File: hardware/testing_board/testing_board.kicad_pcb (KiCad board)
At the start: 2 copper layers, 68 parts, among them J1 Conn_01x04, J10 Conn_01x02, J11 Conn_01x02, J12 Conn_01x02, J13 Conn_01x02, J14 Conn_01x02, J15 Conn_01x02, J16 Conn_01x04, J2 Conn_01x04, J3 Conn_01x04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

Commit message: update testing board
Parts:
- added R26: 330, Resistor_THT:R_Axial_DIN0204_L3.6mm_D1.6mm_P2.54mm_Vertical, F.Cu at (88.3, 8.26)
- R10, R12, R8, R9: value 220 -> 1k
- moved D10 362.0 mm to (-26.7, 12.7), turned to 270 degrees
- moved R16 348.0 mm to (-5.08, 15.2), turned to 90 degrees
- moved D17 340.4 mm to (-17.8, 22.9), turned to 90 degrees
- moved J14 339.3 mm to (-27.9, 30.5), turned to 180 degrees
- moved J7 338.0 mm to (-44.5, 5.08)
- moved D12 334.0 mm to (1.27, 12.7), turned to 270 degrees
- moved J10 333.2 mm to (-2.54, 5.08)
- moved D16 333.1 mm to (-31.8, 22.9), turned to 90 degrees
- moved D11 332.8 mm to (-12.7, 12.7), turned to 270 degrees
- moved R13 331.0 mm to (-47.0, 15.2), turned to 90 degrees
- moved R15 330.4 mm to (-19.1, 15.2), turned to 90 degrees
- moved J9 329.0 mm to (-16.5, 5.08)
- moved R24 328.9 mm to (-11.4, 20.3), turned to 270 degrees
- moved J13 326.4 mm to (-14.0, 30.5), turned to 180 degrees
- moved R23 326.3 mm to (-25.4, 20.3), turned to 270 degrees
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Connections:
- D1 pad 2: Net-(D1-Pad1) -> Net-(D1-Pad2)
- J3 pad 3: +5V -> Net-(J3-Pad3)
- J4 pad 3: +5V -> Net-(J4-Pad3)
- R1 pad 2: Net-(D1-Pad1) -> Net-(D1-Pad2)
- RV1 pad 3: GND -> Net-(R26-Pad2)
- RV2 pad 3: GND -> Net-(R26-Pad2)
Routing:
- net +5V: track 0.00 -> 78.7 mm
- net Net-(R17-Pad2): track 0.00 -> 26.9 mm
- net Net-(J16-Pad2): track 0.00 -> 24.2 mm
- net Net-(R26-Pad2): track 0.00 -> 21.4 mm
- net Net-(D8-Pad2): track 0.00 -> 19.9 mm
- net Net-(D3-Pad2): track 0.00 -> 19.8 mm
- net Net-(D13-Pad2): track 0.00 -> 19.7 mm
- net Net-(J5-Pad2): track 0.00 -> 19.2 mm
- net Net-(D14-Pad2): track 0.00 -> 19.2 mm
- net Net-(J5-Pad1): track 0.00 -> 14.9 mm
- net Net-(J11-Pad1): track 0.00 -> 14.3 mm
- net Net-(J11-Pad2): track 0.00 -> 13.9 mm
- net GND: track 0.00 -> 8.89 mm
- net Net-(J14-Pad1): track 0.00 -> 8.67 mm
- net Net-(J13-Pad1): track 0.00 -> 8.67 mm
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
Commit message: finish prelimary version of training board
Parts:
- removed J10, J11, J12, J13, J14, J15: Conn_01x02, Connector_JST:JST_XH_B2B-XH-A_1x02_P2.50mm_Vertical
- added D19: DIODE, Diode_THT:D_DO-27_P15.24mm_Horizontal, F.Cu at (89.4, 97.4)
- added D20: DIODE, Diode_THT:D_DO-27_P15.24mm_Horizontal, F.Cu at (68.5, 97.4)
- added D21: LED, LED_THT:LED_D3.0mm, F.Cu at (94.6, 132.0)
- added D22: LED, LED_THT:LED_D3.0mm, F.Cu at (72.4, 132.1)
- added R27: 560, Resistor_THT:R_Axial_DIN0204_L3.6mm_D1.6mm_P2.54mm_Vertical, F.Cu at (49.1, 131.7)
- added R28: 560, Resistor_THT:R_Axial_DIN0204_L3.6mm_D1.6mm_P2.54mm_Vertical, F.Cu at (101.0, 132.0)
- added RLY2: G5LE-14_DC5, digikey-footprints:Relay_THT_G5LE-14, F.Cu at (76.1, 105.9)
- added U3: TPIC6595, Package_DIP:DIP-20_W7.62mm_LongPads, F.Cu at (27.9, 104.6)
- J6, J7, J8, J9: value Conn_01x02 -> Conn_01x04; footprint Connector_JST:JST_XH_B2B-XH-A_1x02_P2.50mm_Vertical -> Connector_JST:JST_XH_B4B-XH-A_1x04_P2.50mm_Vertical
- RLY1: value G5V-1-DC12 -> G5LE-14_DC5; footprint digikey-footprints:Relay_THT_G5V-1 -> digikey-footprints:Relay_THT_G5LE-14
- moved J16 184.0 mm to (110.1, 145.4), turned to 90 degrees
- moved R18 182.6 mm to (102.5, 146.7), turned to 0 degrees
- moved U1 175.6 mm to (102.5, 141.6), turned to 90 degrees
- moved J5 172.8 mm to (80.9, 173.9)
- moved U2 172.6 mm to (93.6, 141.6), turned to 90 degrees
- moved R19 159.4 mm to (81.4, 167.0), turned to 90 degrees
- moved R17 158.9 mm to (85.2, 167.0), turned to 90 degrees
- moved R26 158.8 mm to (89.0, 167.0), turned to 90 degrees
- moved RV2 147.0 mm to (80.1, 160.7), turned to 90 degrees
- moved RV1 146.7 mm to (95.4, 160.7), turned to 90 degrees
- moved RLY1 142.4 mm to (97.2, 105.9)
- moved J4 141.6 mm to (23.2, 129.8), turned to 270 degrees
- moved D15 140.4 mm to (61.7, 113.3), turned to 180 degrees
- moved R7 140.0 mm to (28.6, 137.9), turned to 90 degrees
- moved R22 139.6 mm to (60.3, 118.1)
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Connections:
- J2 pad 1: Net-(J2-Pad1) -> Net-(D8-Pad1)
- J2 pad 2: Net-(J2-Pad2) -> Net-(D3-Pad1)
- J7 pad 2: Net-(D9-Pad1) -> Net-(J7-Pad2)
- J8 pad 2: Net-(D10-Pad1) -> Net-(J8-Pad2)
- J9 pad 1: Net-(J9-Pad1) -> Net-(D19-Pad2)
- J9 pad 2: Net-(D11-Pad1) -> Net-(D20-Pad2)
- R10 pad 2: Net-(D8-Pad2) -> Net-(D8-Pad1)
- R11 pad 1: Net-(J2-Pad1) -> Net-(D8-Pad2)
- R11 pad 2: Net-(D8-Pad1) -> Net-(R11-Pad2)
- R13 pad 2: Net-(J7-Pad1) -> +5V
- R14 pad 2: Net-(J8-Pad1) -> +5V
- R15 pad 2: Net-(J9-Pad1) -> +5V
- R16 pad 2: Net-(J10-Pad1) -> +5V
- R20 pad 1: Net-(D13-Pad1) -> Net-(D22-Pad1)
- R20 pad 2: Net-(D14-Pad2) -> GND
- R22 pad 2: Net-(J15-Pad1) -> +5V
- R23 pad 2: Net-(J14-Pad1) -> +5V
- R24 pad 2: Net-(J13-Pad1) -> +5V
- R25 pad 2: Net-(J12-Pad1) -> +5V
- R3 pad 1: Net-(J2-Pad2) -> Net-(R3-Pad1)
- R3 pad 2: Net-(D3-Pad1) -> Net-(D3-Pad2)
- R9 pad 2: Net-(D3-Pad2) -> Net-(D3-Pad1)
- RLY1 pad 1: Net-(RLY1-Pad1) -> +5V
- RLY1 pad 2: Net-(J11-Pad1) -> GND
- RLY1 pad 5: Net-(RLY1-Pad5) -> Net-(D19-Pad2)
- SW3 pad 2: Net-(D3-Pad2) -> Net-(R3-Pad1)
- SW4 pad 2: Net-(D8-Pad2) -> Net-(R11-Pad2)
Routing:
- net +5V: track 78.7 -> 272.0 mm
- net Net-(J7-Pad1): track 8.67 -> 45.7 mm, vias 0 -> 2
- net Net-(D19-Pad2): track 0.00 -> 29.5 mm
- net Net-(D10-Pad1): track 8.16 -> 35.1 mm
- net Net-(D9-Pad1): track 8.16 -> 33.8 mm, vias 0 -> 1
- net Net-(J7-Pad2): track 0.00 -> 22.2 mm
- net Net-(D11-Pad1): track 8.16 -> 30.0 mm
- net Net-(R2-Pad2): track 0.00 -> 21.5 mm
- net Net-(R1-Pad1): track 0.00 -> 21.3 mm
- net Net-(D20-Pad2): track 0.00 -> 21.2 mm
- net Net-(R3-Pad1): track 0.00 -> 18.7 mm
- net Net-(R11-Pad2): track 0.00 -> 18.6 mm
- net Net-(D12-Pad1): track 8.16 -> 26.7 mm
- net Net-(D2-Pad1): track 0.00 -> 16.8 mm
- net Net-(D1-Pad1): track 0.00 -> 15.9 mm
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- added copper zone on B.Cu, net GND
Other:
- board outline added: 100.6 x 99.1 mm

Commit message: update testing board and start work on piezo amplifier
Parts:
- D19, D20: value DIODE -> D_Schottky; footprint Diode_THT:D_DO-27_P15.24mm_Horizontal -> Diode_THT:D_DO-201AE_P15.24mm_Horizontal
- moved D20 15.4 mm to (83.8, 97.8), turned to 180 degrees
- moved D19 15.0 mm to (104.4, 97.8), turned to 180 degrees
- moved R21 5.25 mm to (51.8, 131.6), turned to 180 degrees
- moved R27 4.97 mm to (51.8, 135.9), turned to 180 degrees
- moved D14 2.29 mm to (43.9, 131.3), turned to 90 degrees
- moved D13 0.25 mm to (43.9, 135.6)
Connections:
- D19 pad 1: GND -> Net-(D19-Pad1)
- D19 pad 2: Net-(D19-Pad2) -> GND
- D20 pad 1: GND -> Net-(D20-Pad1)
- D20 pad 2: Net-(D20-Pad2) -> GND
- J6 pad 1: Net-(D13-Pad2) -> Net-(D14-Pad1)
- J6 pad 2: Net-(D14-Pad2) -> Net-(D13-Pad1)
- J9 pad 1: Net-(D19-Pad2) -> Net-(D19-Pad1)
- J9 pad 2: Net-(D20-Pad2) -> Net-(D20-Pad1)
- R21 pad 1: Net-(D14-Pad1) -> Net-(D13-Pad1)
- R21 pad 2: Net-(D13-Pad2) -> Net-(D14-Pad2)
- R27 pad 1: Net-(D13-Pad1) -> Net-(D14-Pad1)
- R27 pad 2: Net-(D14-Pad2) -> Net-(D13-Pad2)
- RLY1 pad 5: Net-(D19-Pad2) -> Net-(D19-Pad1)
- RLY2 pad 5: Net-(D20-Pad2) -> Net-(D20-Pad1)
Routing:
- net Net-(D19-Pad2): track 29.5 -> 0.00 mm
- net Net-(D19-Pad1): track 0.00 -> 28.9 mm
- net Net-(D20-Pad2): track 21.2 -> 0.00 mm
- net Net-(D20-Pad1): track 0.00 -> 21.2 mm
- net Net-(D14-Pad2): track 16.7 -> 6.49 mm
- net Net-(D13-Pad1): track 6.73 -> 16.6 mm
- net Net-(D13-Pad2): track 15.5 -> 6.28 mm
- net Net-(D14-Pad1): track 19.3 -> 16.0 mm

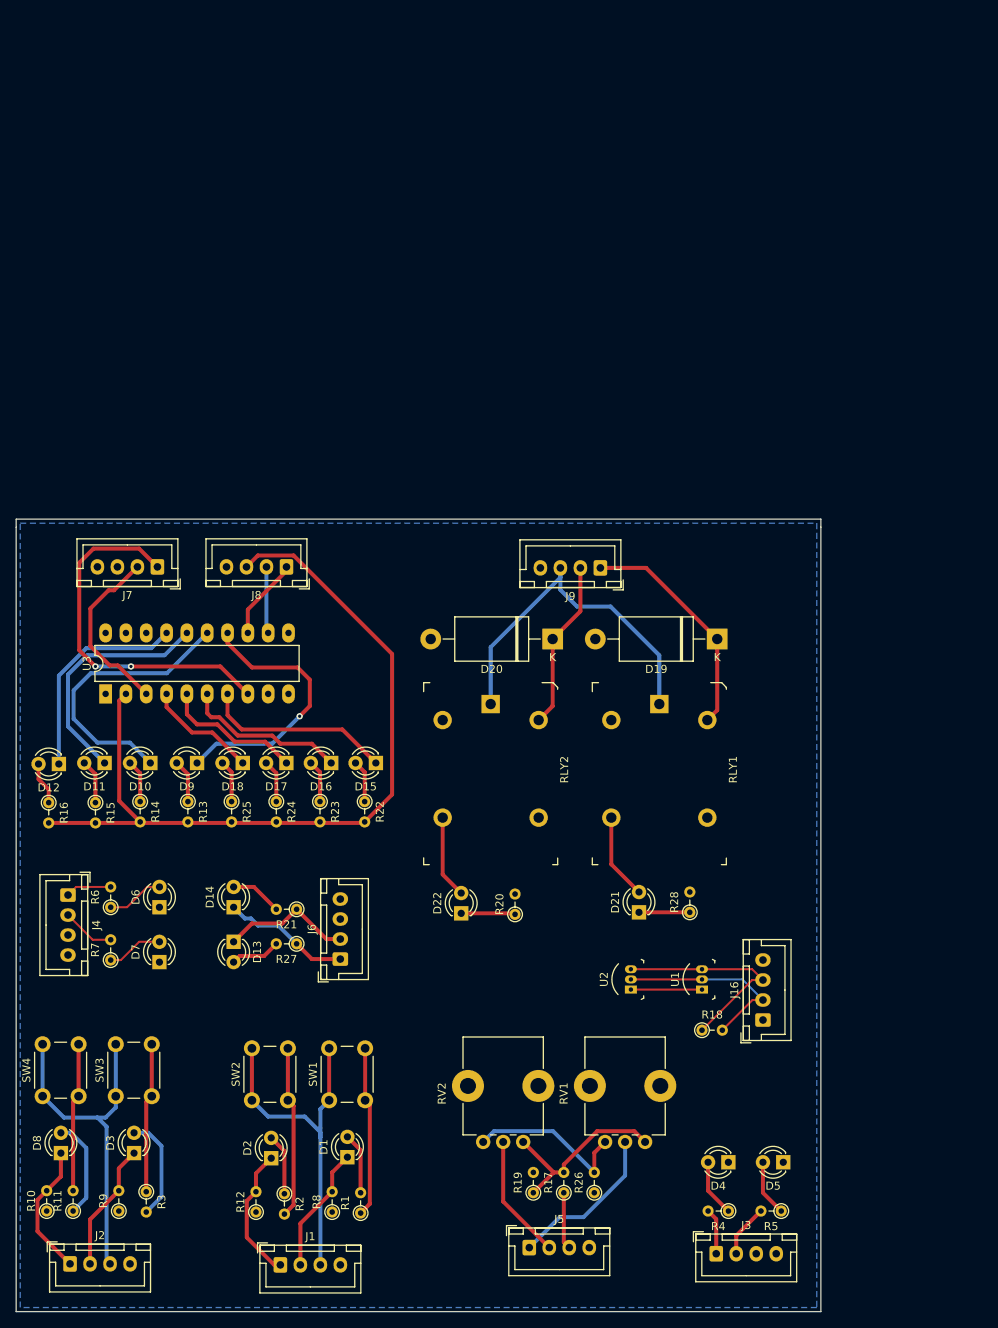
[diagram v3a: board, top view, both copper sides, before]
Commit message: Add mounting holes and spacers
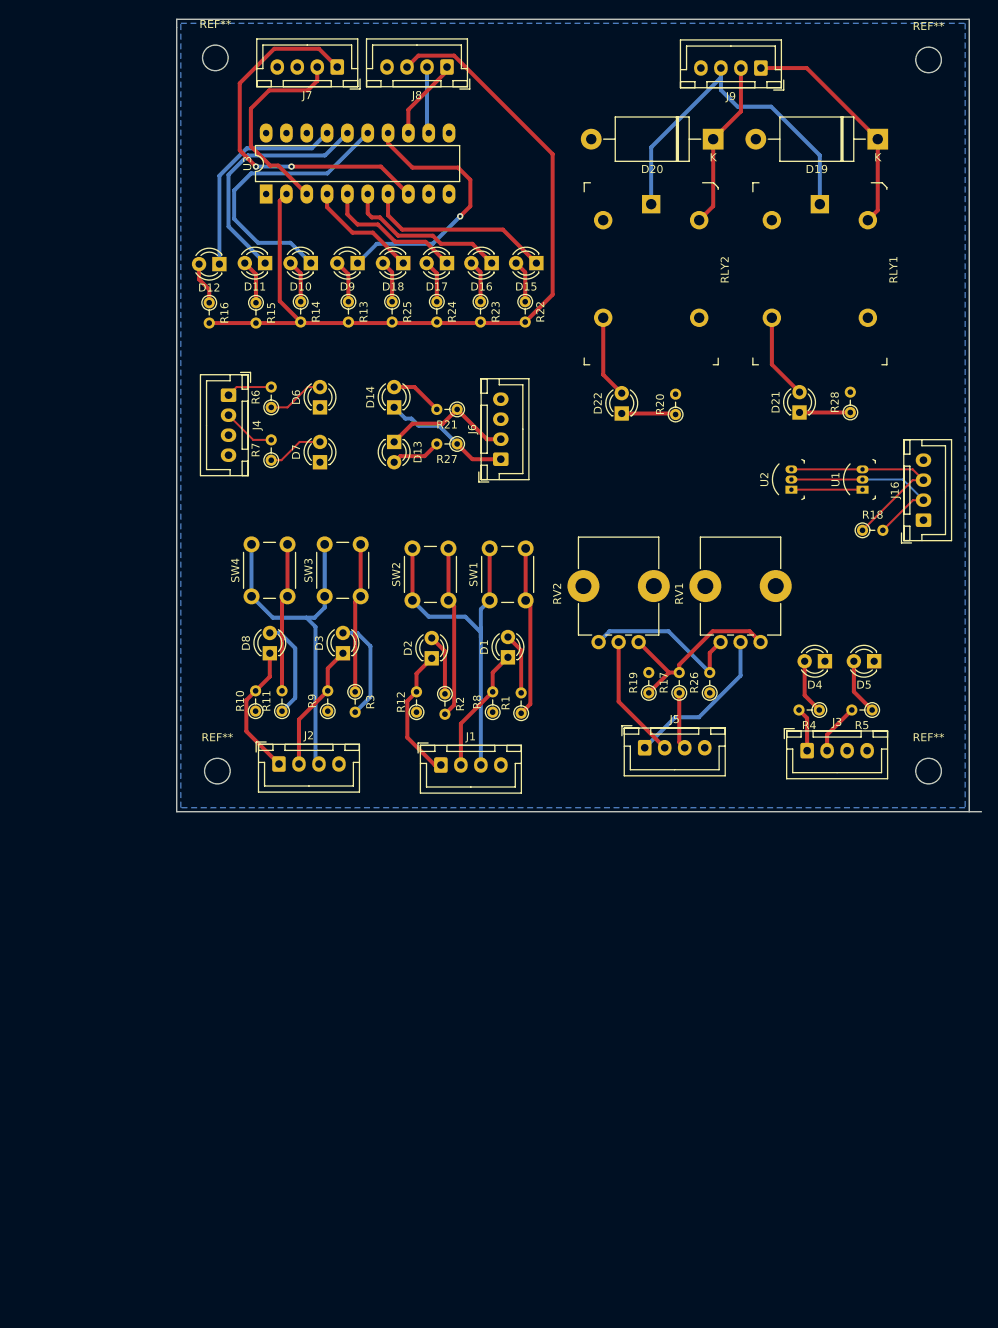
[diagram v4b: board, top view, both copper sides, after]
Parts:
- added REF**: MountingHole_3.2mm_M3, MountingHole:MountingHole_3.2mm_M3, F.Cu at (130.8, 114.3)
- added REF**: MountingHole_3.2mm_M3, MountingHole:MountingHole_3.2mm_M3, F.Cu at (130.8, 25.4)
- added REF**: MountingHole_3.2mm_M3, MountingHole:MountingHole_3.2mm_M3, F.Cu at (41.7, 25.1)
- added REF**: MountingHole_3.2mm_M3, MountingHole:MountingHole_3.2mm_M3, F.Cu at (41.9, 114.3)
- moved J2 67.7 mm to (49.6, 113.4)
- moved D3 67.7 mm to (57.6, 99.6)
- moved D8 67.7 mm to (48.5, 99.6)
- moved R10 67.7 mm to (46.7, 106.8)
- moved R11 67.7 mm to (50.0, 106.8)
- moved R9 67.7 mm to (55.7, 106.8)
- moved SW3 67.7 mm to (55.3, 92.5)
- moved SW4 67.7 mm to (46.2, 92.5)
- moved R3 67.7 mm to (59.1, 104.4)
- moved J7 66.4 mm to (56.9, 26.3)
- moved D1 65.6 mm to (78.2, 100.1)
- moved D10 65.6 mm to (53.6, 50.8)
- moved D11 65.6 mm to (47.9, 50.8)
- moved D14 65.6 mm to (64.0, 68.8)
- moved D15 65.6 mm to (81.8, 50.8)
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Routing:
- net Net-(J7-Pad2): track 22.2 -> 25.6 mm
- net Net-(J7-Pad1): track 45.7 -> 46.7 mm
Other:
- outline, holes or cut-outs redrawn
- net class Default removed

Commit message: update training bpoard design
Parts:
- removed REF** (x4): MountingHole_3.2mm_M3, MountingHole:MountingHole_3.2mm_M3
- added H1: MountingHole, MountingHole:MountingHole_3.2mm_M3_DIN965, F.Cu at (41.7, 25.1)
- added H2: MountingHole, MountingHole:MountingHole_3.2mm_M3_DIN965, F.Cu at (130.8, 25.4)
- added H3: MountingHole, MountingHole:MountingHole_3.2mm_M3_DIN965, F.Cu at (41.9, 114.3)
- added H4: MountingHole, MountingHole:MountingHole_3.2mm_M3_DIN965, F.Cu at (130.8, 114.3)
- moved J3 78.0 mm to (43.2, 82.9), turned to -90 degrees
- moved R5 77.1 mm to (48.2, 91.0), turned to 90 degrees
- moved R4 72.4 mm to (48.2, 84.4), turned to 90 degrees
- moved D5 70.3 mm to (54.3, 91.3), turned to 90 degrees
- moved J16 70.1 mm to (88.4, 26.6), turned to 180 degrees
- moved D4 65.4 mm to (54.3, 85.1), turned to 90 degrees
- moved R18 63.8 mm to (82.2, 34.8)
- moved U1 52.4 mm to (84.7, 42.9), turned to 180 degrees
- moved R21 42.7 mm to (48.4, 104.7), turned to 0 degrees
- moved J6 41.5 mm to (42.9, 98.5), turned to -90 degrees
- moved U2 41.3 mm to (84.7, 49.6), turned to 180 degrees
- moved D14 36.9 mm to (56.2, 105.0), turned to -90 degrees
- moved R27 35.8 mm to (48.4, 100.4), turned to 0 degrees
- moved D13 28.6 mm to (56.2, 100.6), turned to 90 degrees
- moved R16 23.2 mm to (56.1, 38.2), turned to 0 degrees
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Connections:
- D10 pad 1: Net-(D10-Pad1) -> Net-(R14-Pad1)
- D10 pad 2: Net-(D10-Pad2) -> +5V
- D11 pad 2: Net-(D11-Pad2) -> +5V
- D12 pad 1: Net-(D12-Pad1) -> Net-(R16-Pad1)
- D12 pad 2: Net-(D12-Pad2) -> +5V
- D13 pad 1: Net-(D13-Pad1) -> GND
- D14 pad 1: Net-(D14-Pad1) -> GND
- D15 pad 2: Net-(D15-Pad2) -> +5V
- D16 pad 2: Net-(D16-Pad2) -> +5V
- D17 pad 2: Net-(D17-Pad2) -> +5V
- D18 pad 1: Net-(D18-Pad1) -> Net-(R25-Pad1)
- D18 pad 2: Net-(D18-Pad2) -> +5V
- D9 pad 2: Net-(D9-Pad2) -> +5V
- J16 pad 1: Net-(J16-Pad1) -> unconnected-(J16-Pad1)
- J3 pad 3: Net-(J3-Pad3) -> +5V
- J4 pad 3: Net-(J4-Pad3) -> +5V
- J6 pad 1: Net-(D14-Pad1) -> Net-(J6-Pad1)
- J6 pad 2: Net-(D13-Pad1) -> Net-(J6-Pad2)
- R13 pad 1: Net-(D9-Pad2) -> Net-(D9-Pad1)
- R13 pad 2: +5V -> Net-(U3-Pad14)
- R14 pad 1: Net-(D10-Pad2) -> Net-(R14-Pad1)
- R14 pad 2: +5V -> Net-(U3-Pad15)
- R15 pad 1: Net-(D11-Pad2) -> Net-(D11-Pad1)
- R15 pad 2: +5V -> Net-(U3-Pad16)
- R16 pad 1: Net-(D12-Pad2) -> Net-(R16-Pad1)
- R16 pad 2: +5V -> Net-(U3-Pad17)
- R21 pad 1: Net-(D13-Pad1) -> Net-(J6-Pad2)
- R22 pad 1: Net-(D15-Pad2) -> Net-(D15-Pad1)
- R22 pad 2: +5V -> Net-(U3-Pad7)
- R23 pad 1: Net-(D16-Pad2) -> Net-(D16-Pad1)
- R23 pad 2: +5V -> Net-(U3-Pad6)
- R24 pad 1: Net-(D17-Pad2) -> Net-(D17-Pad1)
- R24 pad 2: +5V -> Net-(R24-Pad2)
- R25 pad 1: Net-(D18-Pad2) -> Net-(R25-Pad1)
- R25 pad 2: +5V -> Net-(U3-Pad4)
- R27 pad 1: Net-(D14-Pad1) -> Net-(J6-Pad1)
- RLY1 pad 4: Net-(RLY1-Pad4) -> unconnected-(RLY1-Pad4)
- RLY2 pad 4: Net-(RLY2-Pad4) -> unconnected-(RLY2-Pad4)
- U3 pad 14: Net-(D9-Pad1) -> Net-(U3-Pad14)
- U3 pad 15: Net-(D10-Pad1) -> Net-(U3-Pad15)
- U3 pad 16: Net-(D11-Pad1) -> Net-(U3-Pad16)
- U3 pad 17: Net-(D12-Pad1) -> Net-(U3-Pad17)
- U3 pad 18: Net-(U3-Pad18) -> unconnected-(U3-Pad18)
- U3 pad 4: Net-(D18-Pad1) -> Net-(U3-Pad4)
- U3 pad 5: Net-(D17-Pad1) -> Net-(R24-Pad2)
- U3 pad 6: Net-(D16-Pad1) -> Net-(U3-Pad6)
- U3 pad 7: Net-(D15-Pad1) -> Net-(U3-Pad7)
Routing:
- net +5V: track 272.0 -> 192.4 mm
- net Net-(J7-Pad1): track 46.7 -> 0.00 mm, vias 2 -> 0
- net Net-(D10-Pad1): track 35.1 -> 0.00 mm
- net Net-(U3-Pad14): track 0.00 -> 33.5 mm
- net Net-(D9-Pad1): track 33.8 -> 5.10 mm, vias 1 -> 0
- net Net-(U3-Pad15): track 0.00 -> 26.9 mm
- net Net-(D12-Pad1): track 26.7 -> 0.00 mm
- net Net-(J7-Pad2): track 25.6 -> 0.00 mm
- net Net-(D11-Pad1): track 30.0 -> 5.00 mm
- net Net-(D15-Pad1): track 23.7 -> 0.00 mm
- net Net-(D16-Pad1): track 20.5 -> 0.00 mm
- net Net-(U3-Pad16): track 0.00 -> 19.3 mm
- net Net-(D17-Pad1): track 17.5 -> 0.00 mm
- net Net-(D13-Pad1): track 16.6 -> 0.00 mm
- net Net-(D14-Pad1): track 16.0 -> 0.00 mm
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
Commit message: update solenoid driver and training board
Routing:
- net Net-(U3-Pad7): track 0.00 -> 46.0 mm
- net Net-(J8-Pad1): track 0.51 -> 44.5 mm, vias 0 -> 1
- net Net-(U3-Pad6): track 0.00 -> 43.4 mm
- net Net-(J8-Pad2): track 0.00 -> 39.8 mm
- net Net-(R24-Pad2): track 0.00 -> 39.5 mm
- net Net-(U3-Pad4): track 0.00 -> 35.6 mm
- net Net-(J7-Pad1): track 0.00 -> 34.6 mm
- net +5V: track 192.4 -> 216.7 mm
- net Net-(J7-Pad2): track 0.00 -> 20.3 mm
- net Net-(D15-Pad1): track 0.00 -> 5.13 mm
- net Net-(D17-Pad1): track 0.00 -> 5.08 mm
- net Net-(R25-Pad1): track 0.00 -> 5.04 mm
- net Net-(D16-Pad1): track 0.00 -> 5.02 mm
